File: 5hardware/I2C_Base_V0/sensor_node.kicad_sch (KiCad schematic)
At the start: 57 parts, among them J1 USB_C_Receptacle_USB2.0, J2 PJ-320D-A, J3 Conn_02x06_Top_Bottom, J4 Conn_01x19_Socket, J5 Conn_01x19_Socket, J6 Conn_01x06_Socket, P1 S3B-PH-SM4-TB, P2 S4B-PH-SM4-TB, P3 S3B-PH-SM4-TB, Q2 Si2371EDS, Q3 Si2371EDS, SW2 SW_Push, SW3 SW_Push, U1 MCP1700x-330xxTO, U10 ESP-12F, U12 APDS-9960, U14 DS3231M, U3 CR2450, U4 CH32V003F4P6, U5 SHT31-DIS, U6 DS1307Z+, U7 XC6206PxxxMR, U8 TPL5110, U9 BH1750FVI-TR, Y1 Crystal

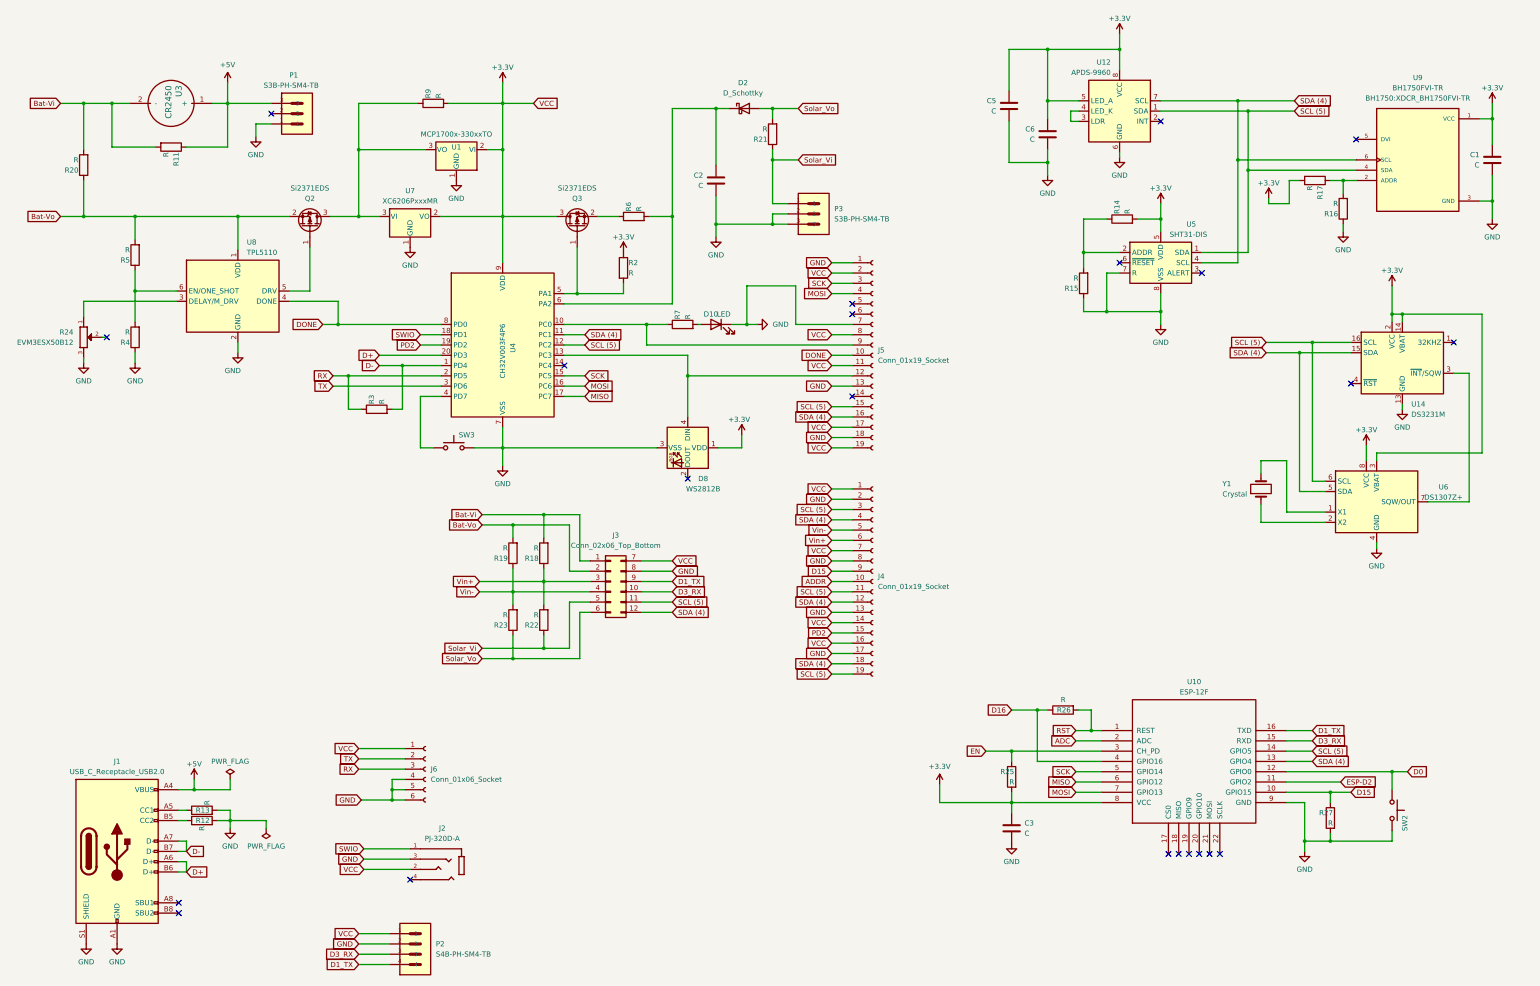
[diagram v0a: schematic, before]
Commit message: update schematic.
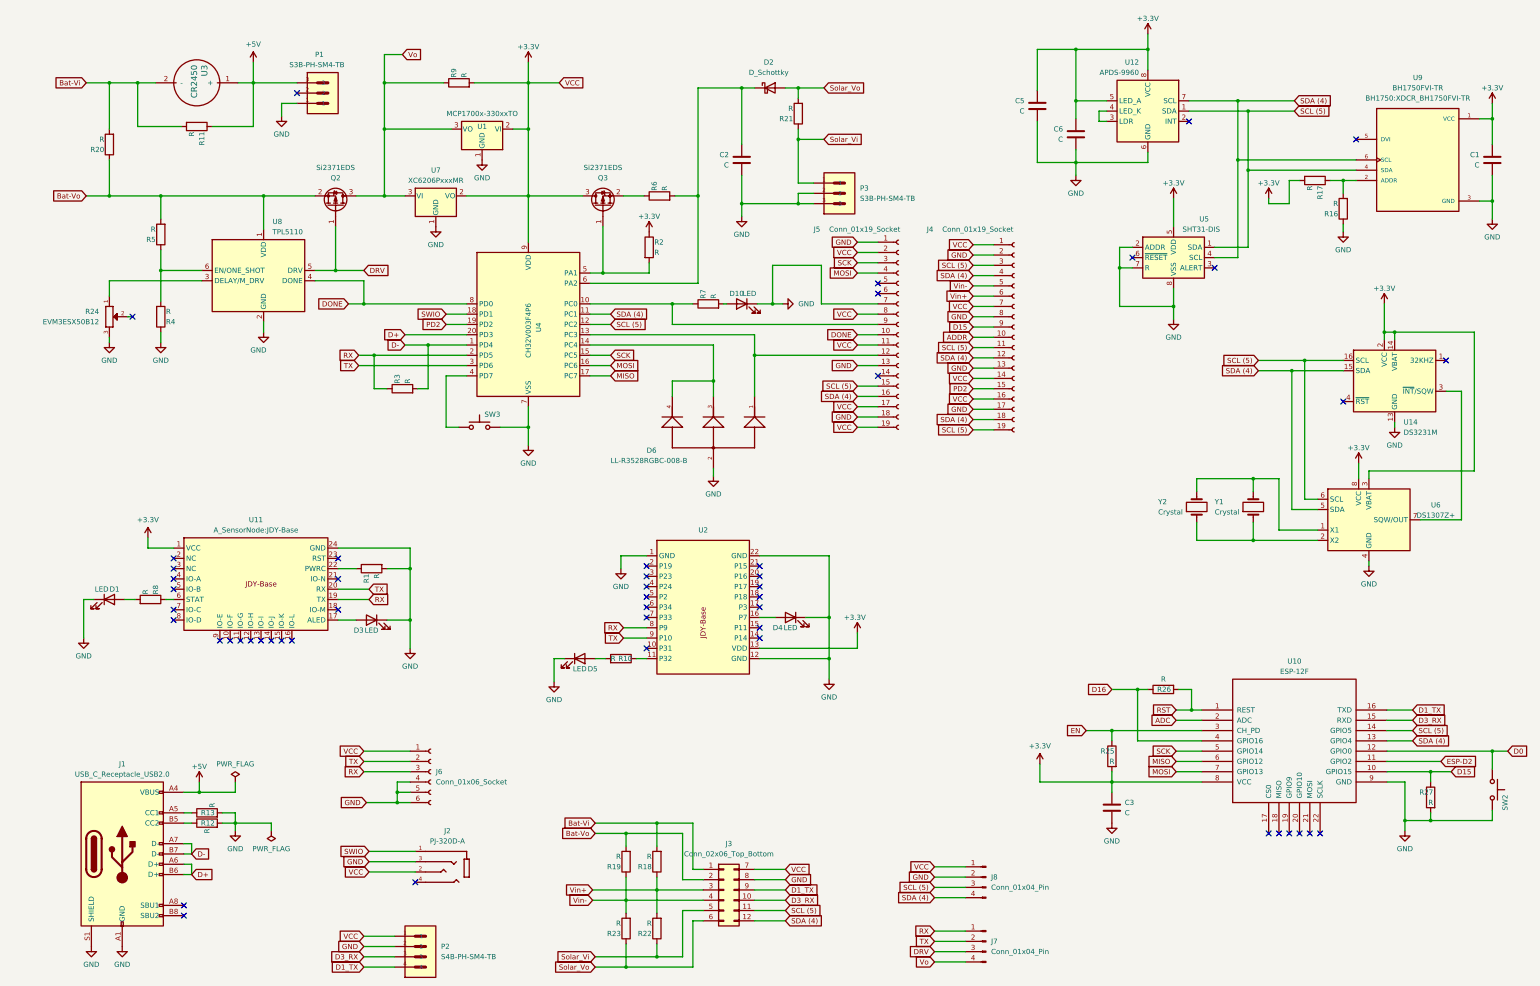
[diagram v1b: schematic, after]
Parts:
- removed D8: WS2812B, LED_SMD:LED_WS2812B_PLCC4_5.0x5.0mm_P3.2mm, symbol LED:WS2812B
- removed R14, R15: R, Resistor_SMD:R_0603_1608Metric, symbol Device:R
- added D1, D3, D4, D5: LED, LED_SMD:LED_0603_1608Metric, symbol Device:LED
- added D6: LL-R3528RGBC-008-B, R3528RGB:LED_LL-R3528RGBC-008-B, symbol R3528RGB:LL-R3528RGBC-008-B
- added J7, J8: Conn_01x04_Pin, Connector_PinHeader_1.27mm:PinHeader_1x04_P1.27mm_Vertical, symbol Connector:Conn_01x04_Pin
- added R1, R10, R8: R, Resistor_SMD:R_0603_1608Metric, symbol Device:R
- added U11: ~, A_SensorNode:JDY-Base, symbol A_SensorNode:JDY-Base
- added U2: ~, A_SensorNode:E104-BT07, symbol A_SensorNode:E104-BT07
- added Y2: Crystal, Crystal:Crystal_Round_D1.5mm_Vertical, symbol Device:Crystal
- D10: footprint LED_SMD:LED_1206_3216Metric -> LED_SMD:LED_0603_1608Metric
- U3: footprint A_SensorNode:CR2450 -> Battery:BatteryHolder_ComfortableElectronic_CH273-2450_1x2450
- Y1: footprint Crystal:Crystal_SMD_0603-2Pin_6.0x3.5mm -> Crystal:Crystal_SMD_3215-2Pin_3.2x1.5mm
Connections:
- net +3.3V: now also J8.1 (Pin_1), U11.1 (VCC), U2.13 (VDD)
- net GND: now also U5.2 (ADDR), D1.1 (K), D3.1 (K), D4.1 (K), D5.1 (K), D6.2, J8.2 (Pin_2), R1.2, U11.24 (GND), U2.1 (GND), U2.12 (GND), U2.22 (GND)
- net RX: now also J7.1 (Pin_1), U11.19 (TX), U2.8 (P9)
- net SCL (5): now also J8.3 (Pin_3)
- net SDA (4): now also J8.4 (Pin_4)
- net TX: now also J7.2 (Pin_2), U11.20 (RX), U2.9 (P10)
- net at J5.12 (Pin_12), U4.13 (PC3): now also D6.1
- net at U6.2 (X2), Y1.1: now also Y2.1
- net at U6.1 (X1), Y1.2: now also Y2.2
- net DRV: now reaches Q2.1 (G), U8.5 (DRV)
- net DRV: now also J7.3 (Pin_3)
- net Vo: now reaches Q2.3 (D), R9.1, U1.3 (VO), U7.3 (VI)
- net Vo: now also J7.4 (Pin_4)
- net at U4.14 (PC4): now also D6.3, D6.4
- new net: D1.2 (A), R8.2
- new net: R1.1, U11.22 (PWRC)
- new net: R10.1, U2.11 (P32)
- new net: D5.2 (A), R10.2
- new net: D4.2 (A), U2.16 (P7)
- new net: R8.1, U11.6 (STAT)
- new net: D3.2 (A), U11.17 (ALED)
- no-connect marks 22 -> 51
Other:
- moved on the sheet: C2, C3, C5, C6, D10, D2, J1, J2, J3, J4, J5, J6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

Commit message: update schematic.
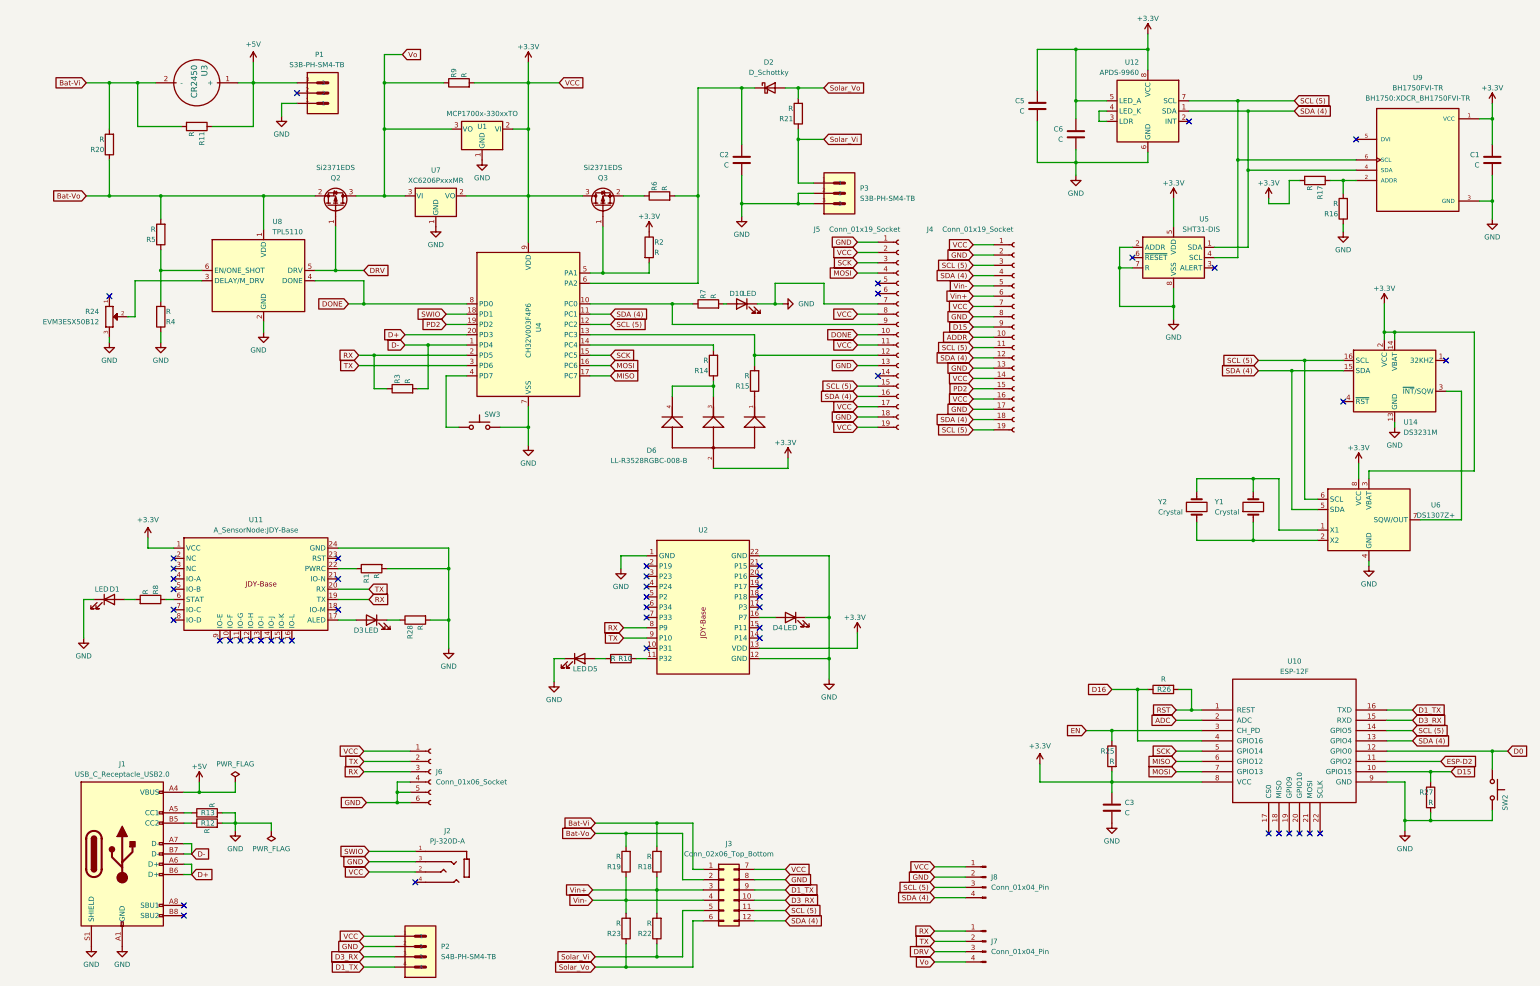
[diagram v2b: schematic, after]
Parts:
- added R14, R15: R, Resistor_SMD:R_1206_3216Metric, symbol Device:R
- added R28: R, Resistor_SMD:R_0805_2012Metric, symbol Device:R
- R10, R7, R8: footprint Resistor_SMD:R_0603_1608Metric -> Resistor_SMD:R_0805_2012Metric
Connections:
- net +3.3V: now also D6.2
- net GND: now also R28.2; no longer D3.1 (K), D6.2
- net SCL (5): now also U12.7 (SCL), U5.4 (SCL), U9.6 (SCL); no longer U12.1 (SDA), U5.1 (SDA), U9.4 (SDA)
- net SDA (4): now also U12.1 (SDA), U5.1 (SDA), U9.4 (SDA); no longer U12.7 (SCL), U5.4 (SCL), U9.6 (SCL)
- net at J5.12 (Pin_12), U4.13 (PC3): now also R15.2; no longer D6.1
- net at U8.3 (DELAY/M_DRV): now also R24.2; no longer R24.1
- net at D6.3, D6.4: now also R14.1; no longer U4.14 (PC4)
- new net: D6.1, R15.1
- new net: D3.1 (K), R28.1
- new net: R14.2, U4.14 (PC4)

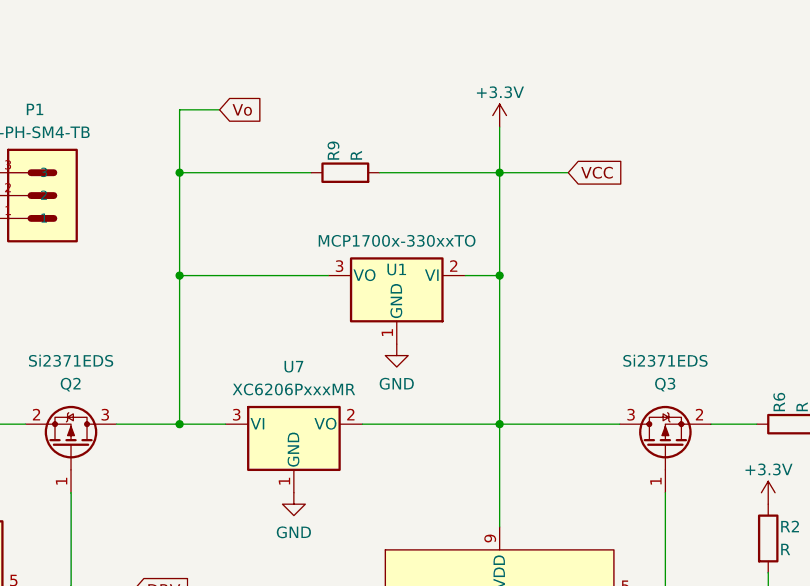
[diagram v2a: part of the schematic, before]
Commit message: update schematic.
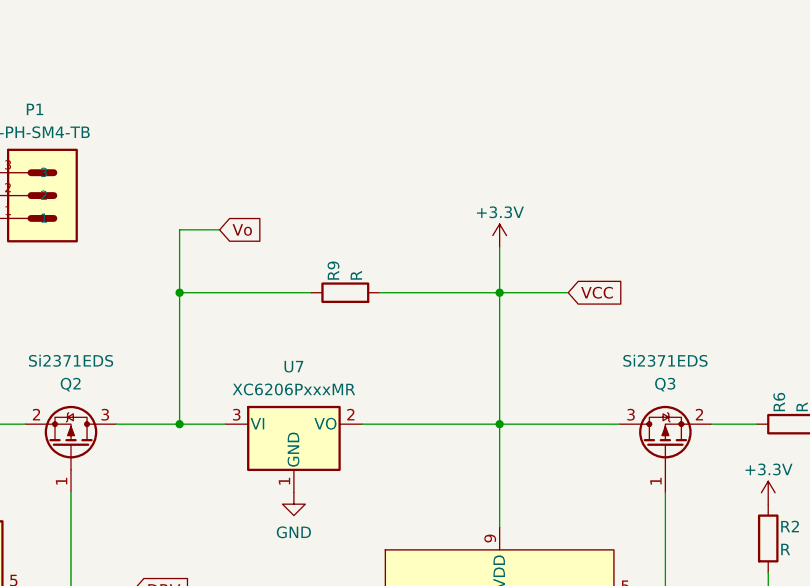
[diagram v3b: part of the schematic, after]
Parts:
- removed U1: MCP1700x-330xxTO, Package_TO_SOT_THT:TO-92_Inline, symbol Regulator_Linear:MCP1700x-330xxTO
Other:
- moved on the sheet: R9
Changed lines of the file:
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@@
   (junction (at 47.625 40.64) (diameter 0) (color 0 0 0 0)
   )
-  (junction (at 115.57 40.64) (diameter 0) (color 0 0 0 0)
+  (junction (at 115.57 53.975) (diameter 0) (color 0 0 0 0)
   )
   (junction (at 367.665 222.885) (diameter 0) (color 0 0 0 0)
@@
   (junction (at 314.96 195.58) (diameter 0) (color 0 0 0 0)
   )
-  (junction (at 151.13 52.07) (diameter 0) (color 0 0 0 0)
-  )
   (junction (at 131.445 173.355) (diameter 0) (color 0 0 0 0)
   )
-  (junction (at 115.57 52.07) (diameter 0) (color 0 0 0 0)
-  )
   (junction (at 310.515 95.885) (diameter 0) (color 0 0 0 0)
   )
@@
   (junction (at 175.26 259.08) (diameter 0) (color 0 0 0 0)
   )
-  (junction (at 151.13 40.64) (diameter 0) (color 0 0 0 0)
+  (junction (at 151.13 53.975) (diameter 0) (color 0 0 0 0)
   )
   (junction (at 352.425 64.77) (diameter 0) (color 0 0 0 0)
@@
     (stroke (width 0) (type default))
   )
-  (wire (pts (xy 158.75 40.64) (xy 151.13 40.64))
+  (wire (pts (xy 158.75 53.975) (xy 151.13 53.975))
     (stroke (width 0) (type default))
   )
@@
     (stroke (width 0) (type default))
   )
-  (wire (pts (xy 151.13 35.56) (xy 151.13 40.64))
+  (wire (pts (xy 151.13 48.895) (xy 151.13 53.975))
     (stroke (width 0) (type default))
   )
@@
     (stroke (width 0) (type default))
   )
-  (wire (pts (xy 115.57 33.655) (xy 115.57 40.64))
+  (wire (pts (xy 115.57 46.99) (xy 115.57 53.975))
     (stroke (width 0) (type default))
   )
-  (wire (pts (xy 137.795 40.64) (xy 151.13 40.64))
+  (wire (pts (xy 137.795 53.975) (xy 151.13 53.975))
     (stroke (width 0) (type default))
   )
@@
     (stroke (width 0) (type default))
   )
-  (wire (pts (xy 115.57 40.64) (xy 115.57 52.07))
+  (wire (pts (xy 115.57 53.975) (xy 115.57 68.58))
     (stroke (width 0) (type default))
   )
@@
     (stroke (width 0) (type default))
   )
-  (wire (pts (xy 151.13 52.07) (xy 151.13 68.58))
-    (stroke (width 0) (type default))
-  )
   (wire (pts (xy 225.425 157.48) (xy 225.425 172.72))
     (stroke (width 0) (type default))
@@
     (stroke (width 0) (type default))
   )
-  (wire (pts (xy 115.57 52.07) (xy 115.57 68.58))
-    (stroke (width 0) (type default))
-  )
   (wire (pts (xy 169.545 76.2) (xy 169.545 87.63))
     (stroke (width 0) (type default))
@@
     (stroke (width 0) (type default))
   )
-  (wire (pts (xy 115.57 40.64) (xy 130.175 40.64))
+  (wire (pts (xy 115.57 53.975) (xy 130.175 53.975))
     (stroke (width 0) (type default))
   )
@@
     (stroke (width 0) (type default))
   )
-  (wire (pts (xy 147.32 52.07) (xy 151.13 52.07))
-    (stroke (width 0) (type default))
-  )
   (wire (pts (xy 311.785 190.5) (xy 314.96 190.5))
     (stroke (width 0) (type default))
@@
     (stroke (width 0) (type default))
   )
-  (wire (pts (xy 115.57 52.07) (xy 132.08 52.07))
-    (stroke (width 0) (type default))
-  )
   (wire (pts (xy 232.41 125.73) (xy 237.49 125.73))
     (stroke (width 0) (type default))
@@
     (stroke (width 0) (type default))
   )
-  (wire (pts (xy 151.13 40.64) (xy 151.13 52.07))
+  (wire (pts (xy 151.13 53.975) (xy 151.13 68.58))
     (stroke (width 0) (type default))
   )
@@
     (stroke (width 0) (type default))
   )
-  (wire (pts (xy 120.015 33.655) (xy 115.57 33.655))
+  (wire (pts (xy 120.015 46.99) (xy 115.57 46.99))
     (stroke (width 0) (type default))
   )
@@
     (stroke (width 0) (type default))
   )
-  (global_label "Vo" (shape input) (at 120.015 33.655 0) (fields_autoplaced)
+  (global_label "Vo" (shape input) (at 120.015 46.99 0) (fields_autoplaced)
     (effects (font (size 1.27 1.27)) (justify left))
-    (property "Intersheetrefs" "${INTERSHEET_REFS}" (at 125.2378 33.655 0)
+    (property "Intersheetrefs" "${INTERSHEET_REFS}" (at 125.2378 46.99 0)
       (effects (font (size 1.27 1.27)) (justify left) hide)
     )
@@
     )
   )
-  (global_label "VCC" (shape input) (at 158.75 40.64 0) (fields_autoplaced)
+  (global_label "VCC" (shape input) (at 158.75 53.975 0) (fields_autoplaced)
     (effects (font (size 1.27 1.27)) (justify left))
-    (property "Intersheetrefs" "${INTERSHEET_REFS}" (at 165.3638 40.64 0)
+    (property "Intersheetrefs" "${INTERSHEET_REFS}" (at 165.3638 53.975 0)
       (effects (font (size 1.27 1.27)) (justify left) hide)
     )
@@
     )
   )
-  (symbol (lib_id "Device:R") (at 133.985 40.64 90) (unit 1)
+  (symbol (lib_id "Device:R") (at 133.985 53.975 90) (unit 1)
     (in_bom yes) (on_board yes) (dnp no)
-    (property "Reference" "R9" (at 132.715 39.37 0)
+    (property "Reference" "R9" (at 132.715 52.705 0)
       (effects (font (size 1.27 1.27)) (justify left))
     )
-    (property "Value" "R" (at 135.255 39.37 0)
+    (property "Value" "R" (at 135.255 52.705 0)
       (effects (font (size 1.27 1.27)) (justify left))
     )
-    (property "Footprint" "Resistor_SMD:R_0603_1608Metric" (at 133.985 42.418 90)
+    (property "Footprint" "Resistor_SMD:R_0603_1608Metric" (at 133.985 55.753 90)
       (effects (font (size 1.27 1.27)) hide)
     )
-    (property "Datasheet" "~" (at 133.985 40.64 0)
+    (property "Datasheet" "~" (at 133.985 53.975 0)
       (effects (font (size 1.27 1.27)) hide)
     )
@@
     )
   )
-  (symbol (lib_id "power:GND") (at 139.7 59.69 0) (mirror y) (unit 1)
-    (in_bom yes) (on_board yes) (dnp no)
-    (property "Reference" "#PWR02" (at 139.7 66.04 0)
-      (effects (font (size 1.27 1.27)) hide)
-    )
-    (property "Value" "GND" (at 139.7 64.135 0)
-      (effects (font (size 1.27 1.27)))
-    )
-    (property "Footprint" "" (at 139.7 59.69 0)
-      (effects (font (size 1.27 1.27)) hide)
-    )
-    (property "Datasheet" "" (at 139.7 59.69 0)
-      (effects (font (size 1.27 1.27)) hide)
-    )
-    (pin "1")
-    (instances
-      (project "sensor_node"
-        (path "/af3a10dd-48b4-4881-8409-82af1b899ed6"
-          (reference "#PWR02") (unit 1)
-        )
-      )
-    )
-  )
   (symbol (lib_id "power:GND") (at 352.425 77.47 0) (mirror y) (unit 1)
     (in_bom yes) (on_board yes) (dnp no) (fields_autoplaced)
@@
     )
   )
-  (symbol (lib_id "power:+3.3V") (at 151.13 35.56 0) (unit 1)
+  (symbol (lib_id "power:+3.3V") (at 151.13 48.895 0) (unit 1)
     (in_bom yes) (on_board yes) (dnp no)
-    (property "Reference" "#PWR04" (at 151.13 39.37 0)
+    (property "Reference" "#PWR04" (at 151.13 52.705 0)
       (effects (font (size 1.27 1.27)) hide)
     )
-    (property "Value" "+3.3V" (at 151.13 31.75 0)
+    (property "Value" "+3.3V" (at 151.13 45.085 0)
       (effects (font (size 1.27 1.27)))
     )
-    (property "Footprint" "" (at 151.13 35.56 0)
+    (property "Footprint" "" (at 151.13 48.895 0)
       (effects (font (size 1.27 1.27)) hide)
     )
-    (property "Datasheet" "" (at 151.13 35.56 0)
+    (property "Datasheet" "" (at 151.13 48.895 0)
       (effects (font (size 1.27 1.27)) hide)
     )
@@
         )
       )
-    )
-  )
-  (symbol (lib_id "Regulator_Linear:MCP1700x-330xxTO") (at 139.7 52.07 180) (unit 1)
-    (in_bom yes) (on_board yes) (dnp no)
-    (property "Reference" "U1" (at 139.7 51.435 0)
-      (effects (font (size 1.27 1.27)))
-    )
-    (property "Value" "MCP1700x-330xxTO" (at 139.7 48.26 0)
-      (effects (font (size 1.27 1.27)))
-    )
-    (property "Footprint" "Package_TO_SOT_THT:TO-92_Inline" (at 139.7 46.99 0)
-      (effects (font (size 1.27 1.27) italic) hide)
-    )
-    (property "Datasheet" "http://ww1.microchip.com/downloads/en/DeviceDoc/20001826D.pdf" (at 139.7 52.07 0)
-      (effects (font (size 1.27 1.27)) hide)
-    )
-    (pin "1")
-    (pin "2")
-    (pin "3")
-    (instances
-      (project "sensor_node"
-        (path "/af3a10dd-48b4-4881-8409-82af1b899ed6"
-          (reference "U1") (unit 1)
-        )
-      )

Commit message: update pcb.
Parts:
- removed J1: USB_C_Receptacle_USB2.0, Connector_USB:USB_C_Receptacle_GCT_USB4135-GF-A_6P_TopMnt_Horizontal, symbol Connector:USB_C_Receptacle_USB2.0
- removed R12, R13: R, Resistor_SMD:R_1206_3216Metric, symbol Device:R
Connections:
- no-connect marks 51 -> 49
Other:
- moved on the sheet: P1
